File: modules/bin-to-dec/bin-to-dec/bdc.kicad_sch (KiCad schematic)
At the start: 3 parts

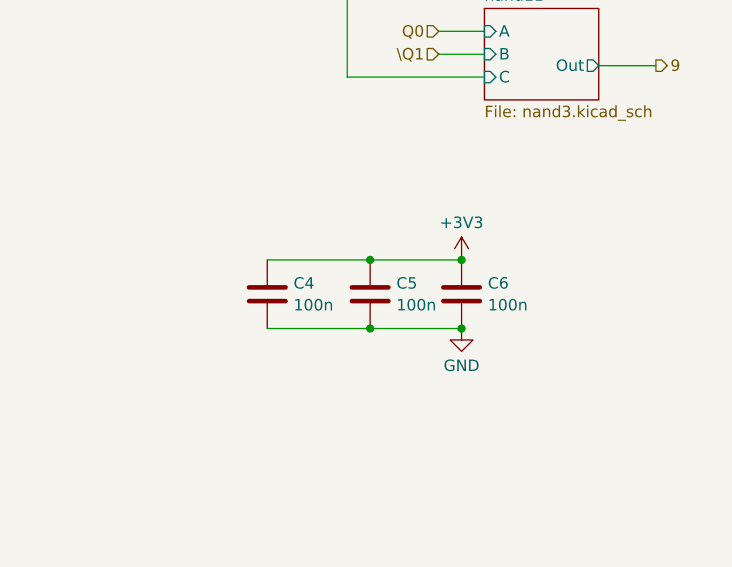
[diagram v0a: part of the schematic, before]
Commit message: routed on bdc
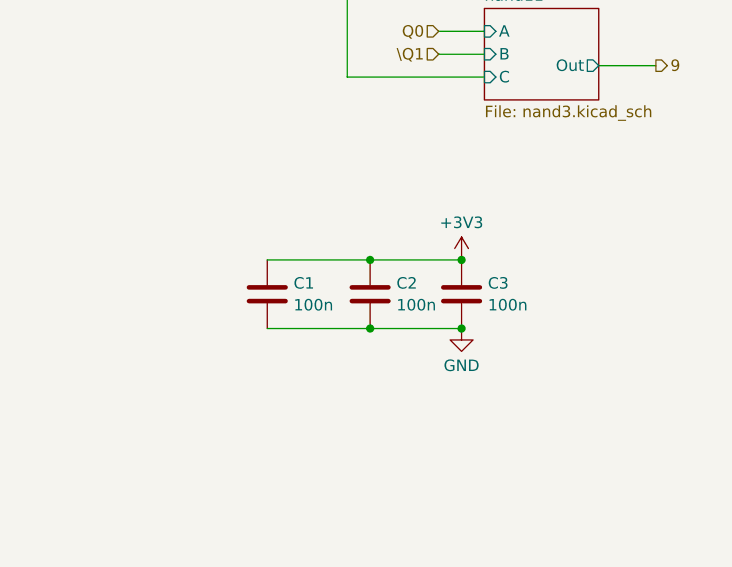
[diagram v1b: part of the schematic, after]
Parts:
- renumbered C4 to C1, C5 to C2, C6 to C3
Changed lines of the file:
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@@
 		(dnp no)
 		(fields_autoplaced yes)
-		(property "Reference" "C4"
+		(property "Reference" "C1"
 			(at 171.831 76.2578 0)
 			(effects
@@
 				(path "/b244e12b-f85f-4579-ba5e-848643f54694/5653fc28-2bc8-4af2-8007-5d6d268cbb44"
 					(reference "C4")
+					(unit 1)
+				)
+				(path "/b244e12b-f85f-4579-ba5e-848643f54694/56916597-06d0-4a11-97bd-1503266c17ac"
+					(reference "C1")
 					(unit 1)
 				)
@@
 		(dnp no)
 		(fields_autoplaced yes)
-		(property "Reference" "C6"
+		(property "Reference" "C3"
 			(at 193.421 76.2578 0)
 			(effects
@@
 				(path "/b244e12b-f85f-4579-ba5e-848643f54694/5653fc28-2bc8-4af2-8007-5d6d268cbb44"
 					(reference "C6")
+					(unit 1)
+				)
+				(path "/b244e12b-f85f-4579-ba5e-848643f54694/56916597-06d0-4a11-97bd-1503266c17ac"
+					(reference "C3")
 					(unit 1)
 				)
@@
 		(dnp no)
 		(fields_autoplaced yes)
-		(property "Reference" "#PWR029"
+		(property "Reference" "#PWR06"
 			(at 190.5 77.47 0)
 			(effects
@@
 				(path "/b244e12b-f85f-4579-ba5e-848643f54694/5653fc28-2bc8-4af2-8007-5d6d268cbb44"
 					(reference "#PWR029")
+					(unit 1)
+				)
+				(path "/b244e12b-f85f-4579-ba5e-848643f54694/56916597-06d0-4a11-97bd-1503266c17ac"
+					(reference "#PWR06")
 					(unit 1)
 				)
@@
 		(dnp no)
 		(fields_autoplaced yes)
-		(property "Reference" "C5"
+		(property "Reference" "C2"
 			(at 183.261 76.2578 0)
 			(effects
@@
 				(path "/b244e12b-f85f-4579-ba5e-848643f54694/5653fc28-2bc8-4af2-8007-5d6d268cbb44"
 					(reference "C5")
+					(unit 1)
+				)
+				(path "/b244e12b-f85f-4579-ba5e-848643f54694/56916597-06d0-4a11-97bd-1503266c17ac"
+					(reference "C2")
 					(unit 1)
 				)
@@
 		(dnp no)
 		(fields_autoplaced yes)
-		(property "Reference" "#PWR030"
+		(property "Reference" "#PWR07"
 			(at 190.5 87.63 0)
 			(effects
@@
 				(path "/b244e12b-f85f-4579-ba5e-848643f54694/5653fc28-2bc8-4af2-8007-5d6d268cbb44"
 					(reference "#PWR030")
+					(unit 1)
+				)
+				(path "/b244e12b-f85f-4579-ba5e-848643f54694/56916597-06d0-4a11-97bd-1503266c17ac"
+					(reference "#PWR07")
 					(unit 1)
 				)
@@
 					(page "19")
 				)
+				(path "/b244e12b-f85f-4579-ba5e-848643f54694/56916597-06d0-4a11-97bd-1503266c17ac"
+					(page "6")
+				)
 			)
 		)
@@
 					(page "29")
 				)
+				(path "/b244e12b-f85f-4579-ba5e-848643f54694/56916597-06d0-4a11-97bd-1503266c17ac"
+					(page "8")
+				)
 			)
 		)
@@
 					(page "25")
 				)
+				(path "/b244e12b-f85f-4579-ba5e-848643f54694/56916597-06d0-4a11-97bd-1503266c17ac"
+					(page "14")
+				)
 			)
 		)
@@
 					(page "4")
 				)
+				(path "/b244e12b-f85f-4579-ba5e-848643f54694/56916597-06d0-4a11-97bd-1503266c17ac"
+					(page "11")
+				)
 			)
 		)
@@
 					(page "22")
 				)
+				(path "/b244e12b-f85f-4579-ba5e-848643f54694/56916597-06d0-4a11-97bd-1503266c17ac"
+					(page "12")
+				)
 			)
 		)
@@
 					(page "20")
 				)
+				(path "/b244e12b-f85f-4579-ba5e-848643f54694/56916597-06d0-4a11-97bd-1503266c17ac"
+					(page "18")
+				)
 			)
 		)
@@
 					(page "27")
 				)
+				(path "/b244e12b-f85f-4579-ba5e-848643f54694/56916597-06d0-4a11-97bd-1503266c17ac"
+					(page "7")
+				)
 			)
 		)
@@
 					(page "21")
 				)
+				(path "/b244e12b-f85f-4579-ba5e-848643f54694/56916597-06d0-4a11-97bd-1503266c17ac"
+					(page "10")
+				)
 			)
 		)
@@
 					(page "28")
 				)
+				(path "/b244e12b-f85f-4579-ba5e-848643f54694/56916597-06d0-4a11-97bd-1503266c17ac"
+					(page "9")
+				)
 			)
 		)
@@
 					(page "24")
 				)
+				(path "/b244e12b-f85f-4579-ba5e-848643f54694/56916597-06d0-4a11-97bd-1503266c17ac"
+					(page "16")
+				)
 			)
 		)
@@
 					(page "26")
 				)
+				(path "/b244e12b-f85f-4579-ba5e-848643f54694/56916597-06d0-4a11-97bd-1503266c17ac"
+					(page "15")
+				)
 			)
 		)
@@
 					(page "5")
 				)
+				(path "/b244e12b-f85f-4579-ba5e-848643f54694/56916597-06d0-4a11-97bd-1503266c17ac"
+					(page "17")
+				)
 			)
 		)
@@
 					(page "23")
 				)
-			)
+				(path "/b244e12b-f85f-4579-ba5e-848643f54694/56916597-06d0-4a11-97bd-1503266c17ac"
+					(page "13")
+				)
+			)
